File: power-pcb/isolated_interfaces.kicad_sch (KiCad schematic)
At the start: 24 parts, among them J10 USB_A, U16 RFM-0505S, U17 RFM-0505S, U18 RFM-0505S, U19 ECMF02-2AMX6, U20 ADUM3160

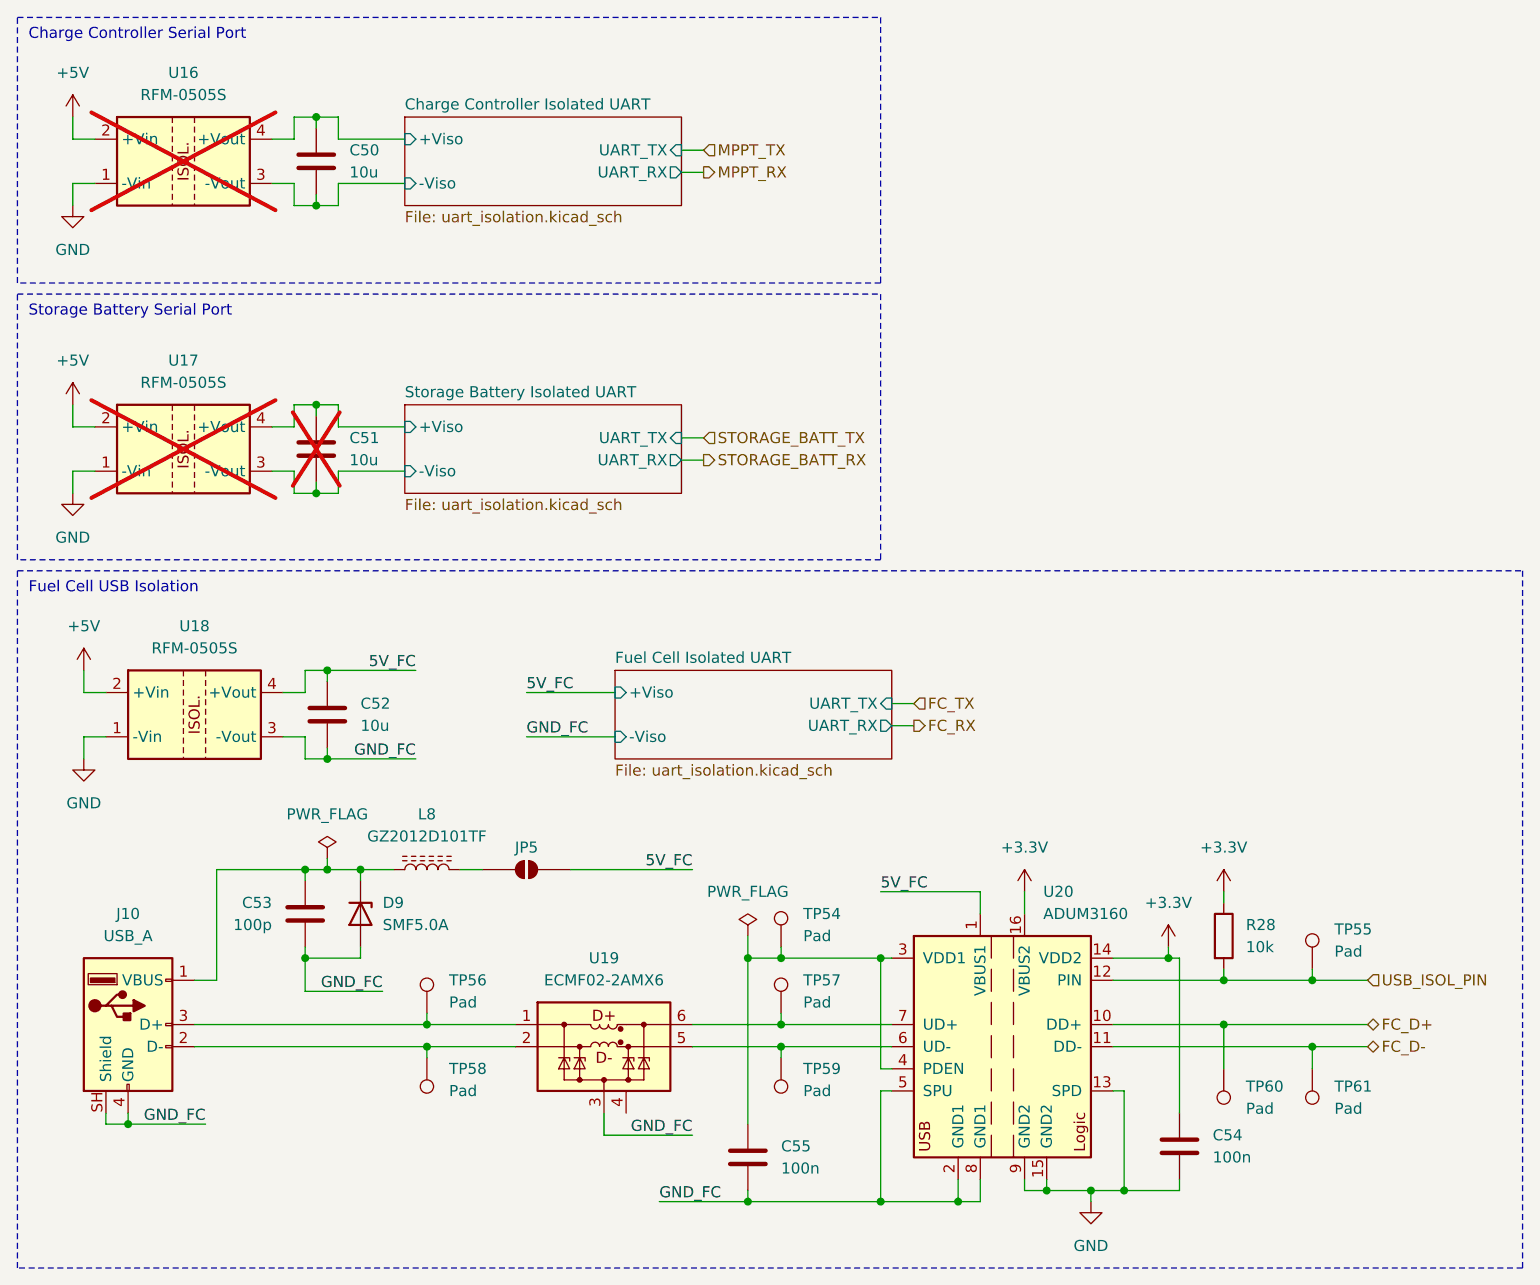
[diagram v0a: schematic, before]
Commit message: power-pcb: re-annotate schematic and start board
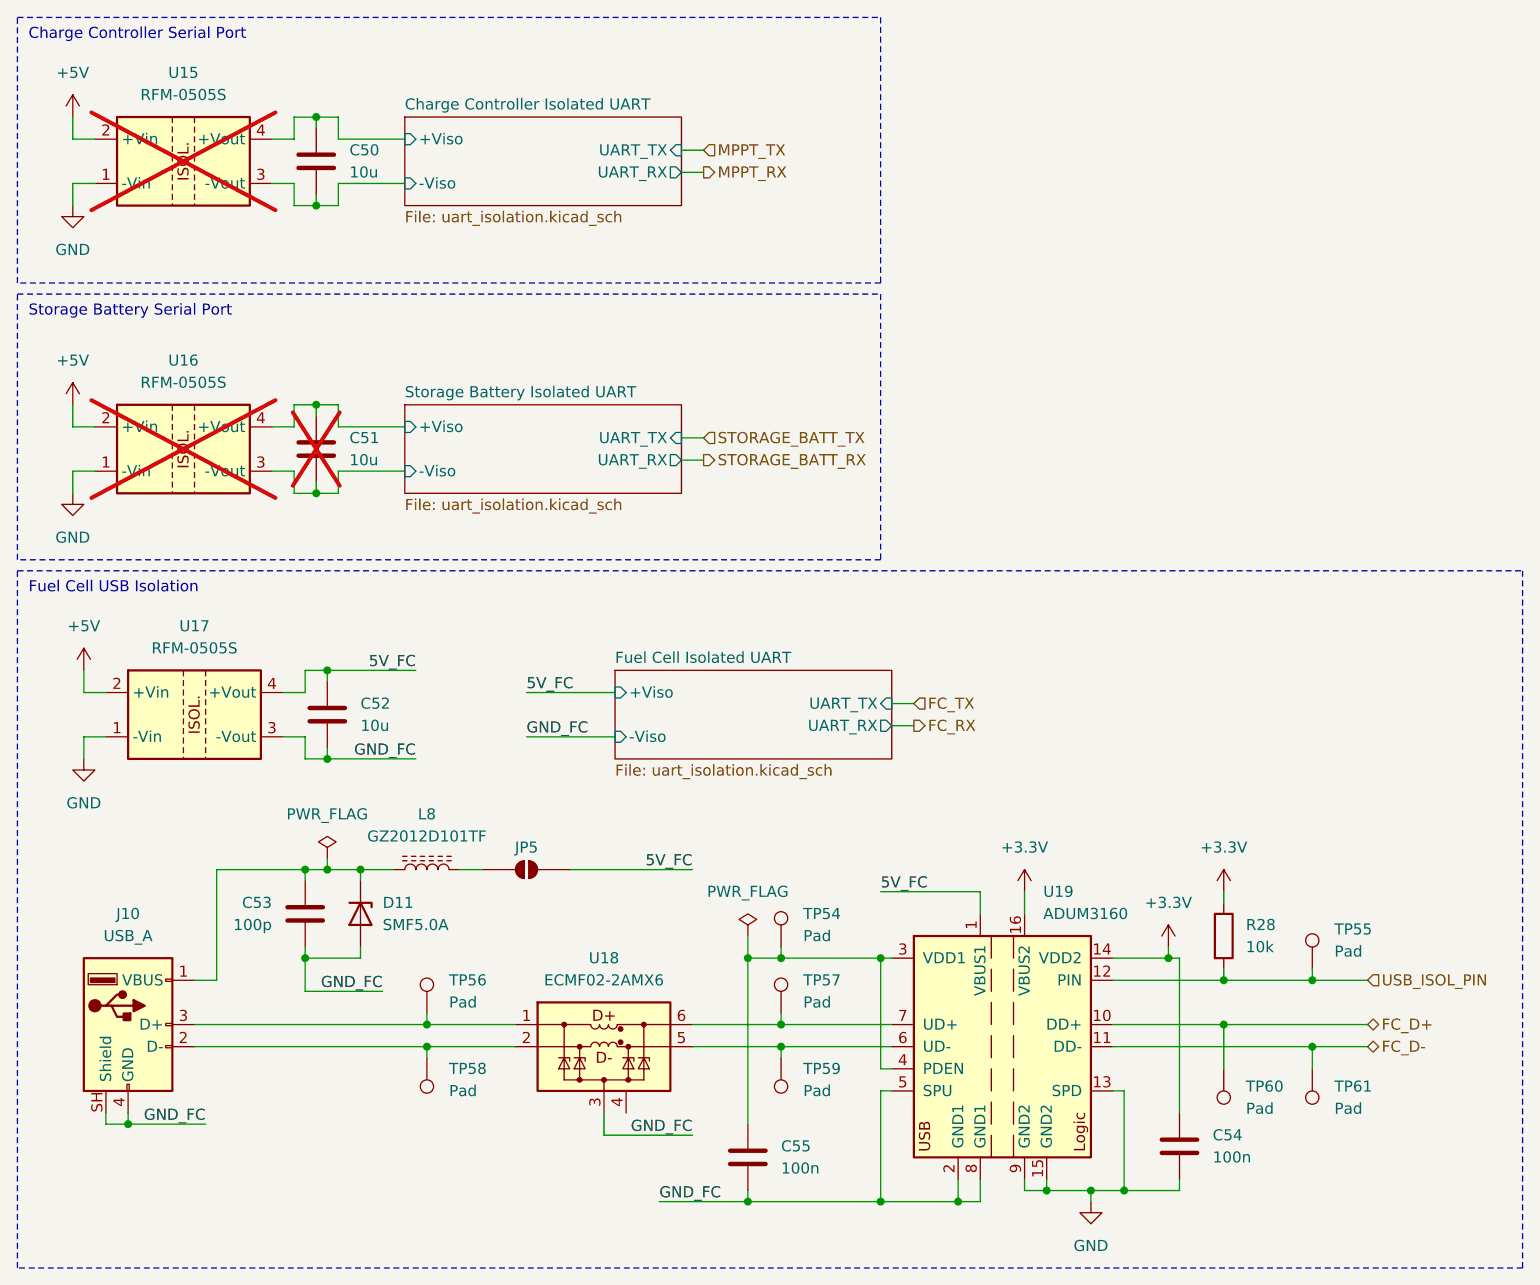
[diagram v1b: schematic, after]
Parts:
- renumbered D9 to D11, U16 to U15, U17 to U16, U18 to U17, U19 to U18, U20 to U19
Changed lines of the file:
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@@
 		(dnp no)
 		(fields_autoplaced yes)
-		(property "Reference" "D9"
+		(property "Reference" "D11"
 			(at 54.61 114.2999 90)
 			(show_name no)
@@
 			(project "power-pcb"
 				(path "/4b4cf3aa-c94c-4150-b9c5-35049cd71136/98c47c69-e753-45d5-a949-1f6e782e8c07"
-					(reference "D9")
+					(reference "D11")
 					(unit 1)
 					(variant
@@
 		(dnp no)
 		(fields_autoplaced yes)
-		(property "Reference" "U19"
+		(property "Reference" "U18"
 			(at 80.01 120.65 0)
 			(show_name no)
@@
 			(project "power-pcb"
 				(path "/4b4cf3aa-c94c-4150-b9c5-35049cd71136/98c47c69-e753-45d5-a949-1f6e782e8c07"
-					(reference "U19")
+					(reference "U18")
 					(unit 1)
 					(variant
@@
 		(dnp no)
 		(fields_autoplaced yes)
-		(property "Reference" "U18"
+		(property "Reference" "U17"
 			(at 33.02 82.55 0)
 			(show_name no)
@@
 			(project "power-pcb"
 				(path "/4b4cf3aa-c94c-4150-b9c5-35049cd71136/98c47c69-e753-45d5-a949-1f6e782e8c07"
-					(reference "U18")
+					(reference "U17")
 					(unit 1)
 					(variant
@@
 		(dnp yes)
 		(fields_autoplaced yes)
-		(property "Reference" "U17"
+		(property "Reference" "U16"
 			(at 31.75 52.07 0)
 			(show_name no)
@@
 			(project "power-pcb"
 				(path "/4b4cf3aa-c94c-4150-b9c5-35049cd71136/98c47c69-e753-45d5-a949-1f6e782e8c07"
-					(reference "U17")
+					(reference "U16")
 					(unit 1)
 					(variant
@@
 		(dnp no)
 		(fields_autoplaced yes)
-		(property "Reference" "U20"
+		(property "Reference" "U19"
 			(at 130.4133 113.03 0)
 			(show_name no)
@@
 			(project "power-pcb"
 				(path "/4b4cf3aa-c94c-4150-b9c5-35049cd71136/98c47c69-e753-45d5-a949-1f6e782e8c07"
-					(reference "U20")
+					(reference "U19")
 					(unit 1)
 					(variant
@@
 		(dnp yes)
 		(fields_autoplaced yes)
-		(property "Reference" "U16"
+		(property "Reference" "U15"
 			(at 31.75 19.05 0)
 			(show_name no)
@@
 			(project "power-pcb"
 				(path "/4b4cf3aa-c94c-4150-b9c5-35049cd71136/98c47c69-e753-45d5-a949-1f6e782e8c07"
-					(reference "U16")
+					(reference "U15")
 					(unit 1)
 					(variant

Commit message: power-pcb: fix schematic after review
- Add footprint for resitive load for the RECOM
- Add Opamps when useful
- Add capacitor and change some footprint sizes
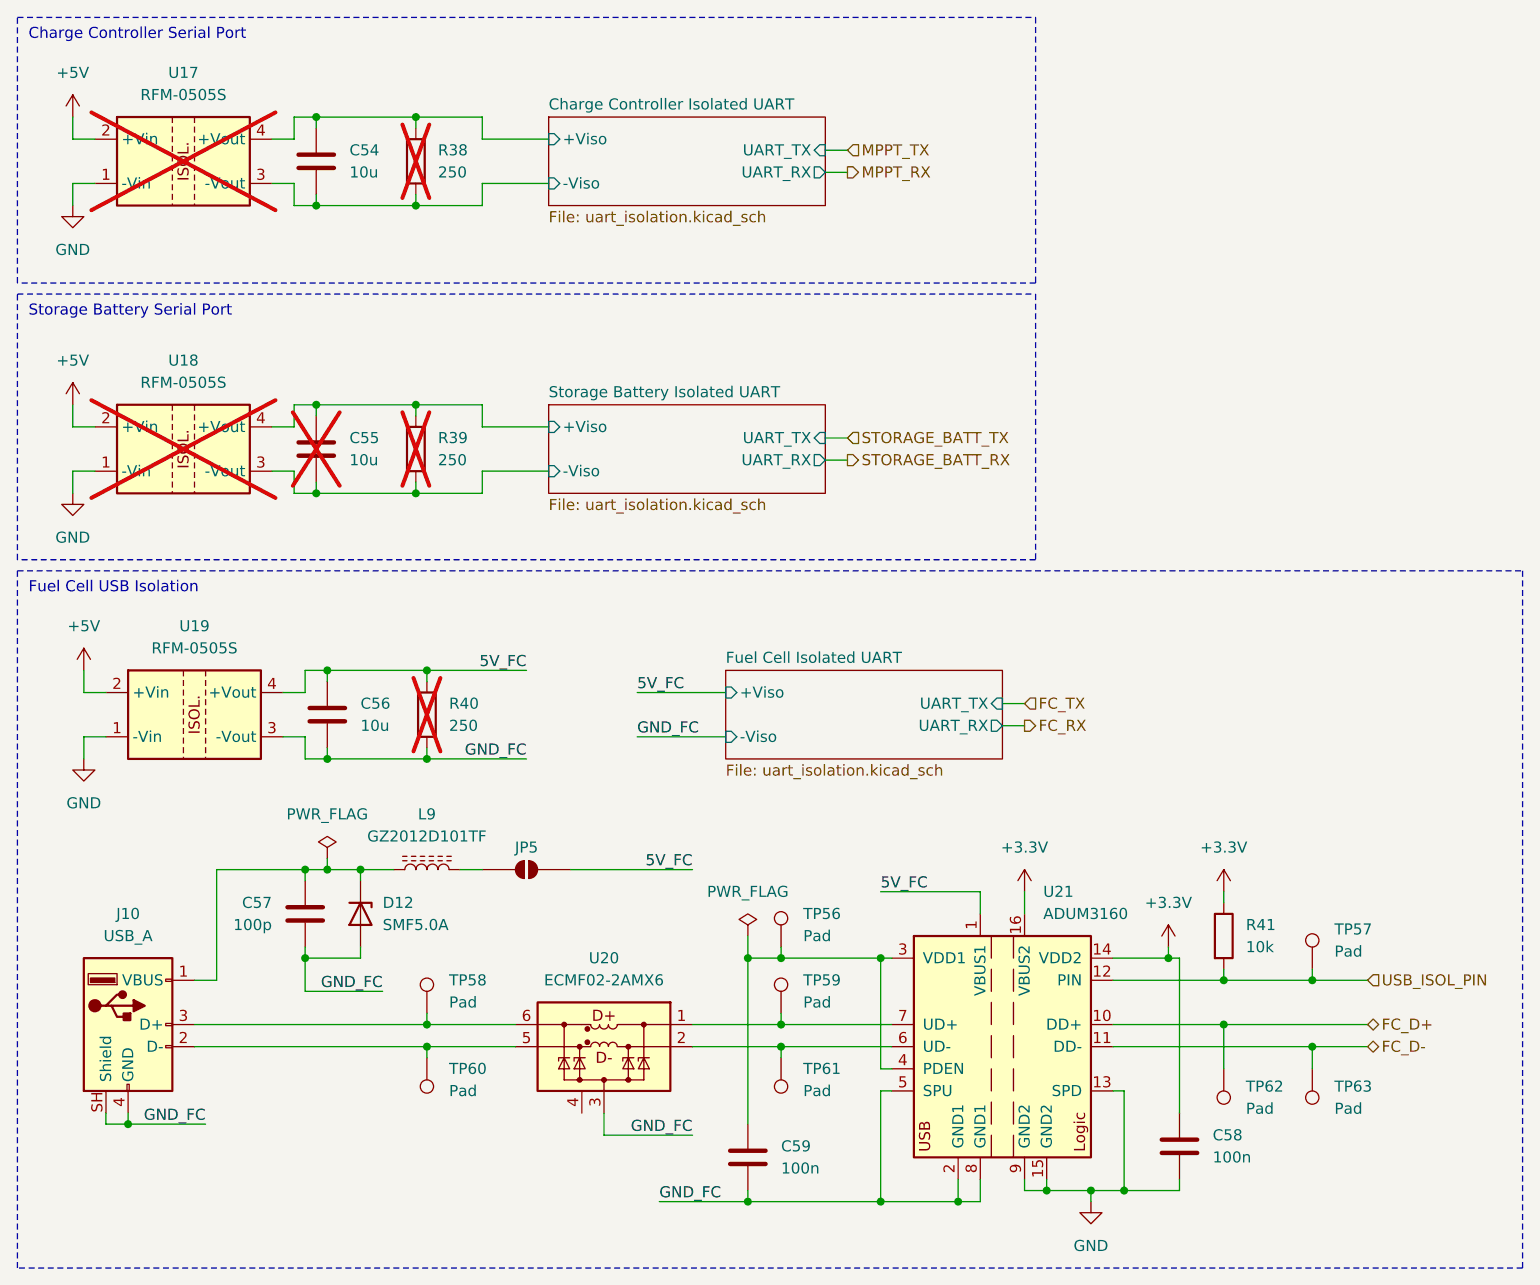
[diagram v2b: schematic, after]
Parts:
- added R38, R39, R40: 250, Resistor_THT:R_Axial_DIN0309_L9.0mm_D3.2mm_P12.70mm_Horizontal, symbol Device:R
- C58: renamed from C54; footprint Capacitor_SMD:C_0603_1608Metric_Pad1.08x0.95mm_HandSolder -> Capacitor_SMD:C_0402_1005Metric_Pad0.74x0.62mm_HandSolder; JLCPCB C14663 -> C307331
- C59: renamed from C55; footprint Capacitor_SMD:C_0603_1608Metric_Pad1.08x0.95mm_HandSolder -> Capacitor_SMD:C_0402_1005Metric_Pad0.74x0.62mm_HandSolder; JLCPCB C14663 -> C307331
- renumbered C50 to C54, C51 to C55, C52 to C56, C53 to C57, D11 to D12, L8 to L9, R28 to R41, TP54 to TP56, TP55 to TP57, TP56 to TP58, TP57 to TP59, TP58 to TP60, TP59 to TP61, TP60 to TP62, TP61 to TP63, U15 to U17, U16 to U18, U17 to U19, U18 to U20, U19 to U21
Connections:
- net 5V_FC: now also R40.1
- net Charge Controller Isolated UART/+Viso: now also R38.1
- net Charge Controller Isolated UART/-Viso: now also R38.2
- net GND_FC: now also R40.2
- net Storage Battery Isolated UART/+Viso: now also R39.1
- net Storage Battery Isolated UART/-Viso: now also R39.2
- net at J10.3 (D+), TP58.1: now also U20.6 (D+_out); no longer U20.1 (D+_in)
- net at J10.2 (D-), TP60.1: now also U20.5 (D-_out); no longer U20.2 (D-_in)
- net at TP61.1, U21.6 (UD-): now also U20.2 (D-_in); no longer U20.5 (D-_out)
- net at TP59.1, U21.7 (UD+): now also U20.1 (D+_in); no longer U20.6 (D+_out)

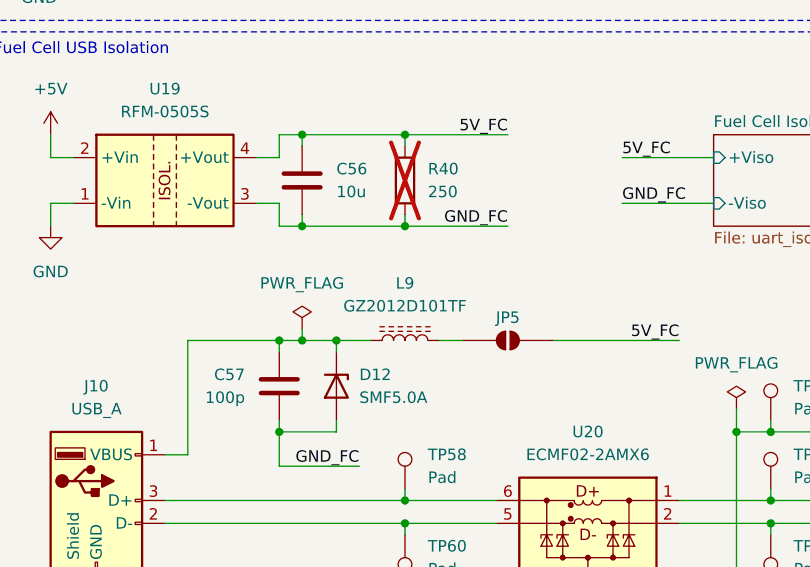
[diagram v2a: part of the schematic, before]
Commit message: power-pcb: work on part placement and JLCPCB DNP
Some of the components that were recentlt added had not been marked as
DNP for JLCPCB yet, this is now done.
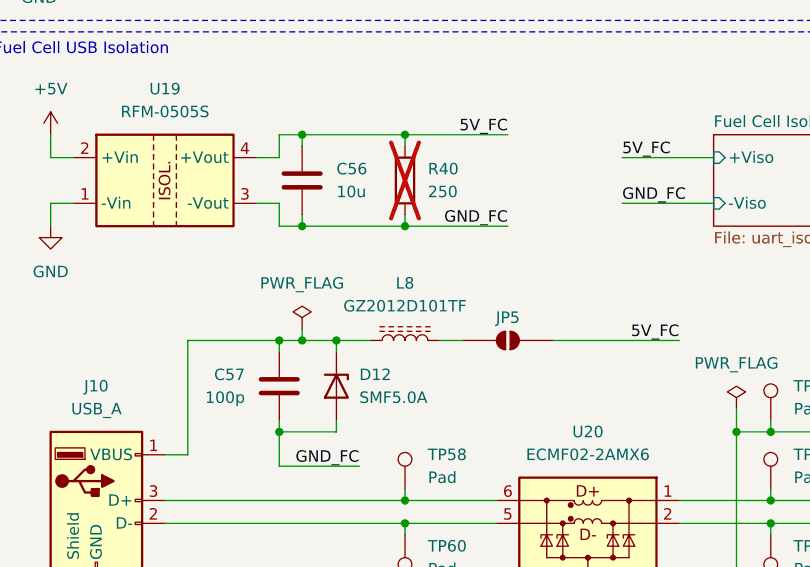
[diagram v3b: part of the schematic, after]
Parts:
- renumbered L9 to L8
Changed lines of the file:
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@@
 		(dnp no)
 		(fields_autoplaced yes)
-		(property "Reference" "L9"
+		(property "Reference" "L8"
 			(at 59.69 104.14 90)
 			(show_name no)
@@
 			(project "power-pcb"
 				(path "/4b4cf3aa-c94c-4150-b9c5-35049cd71136/98c47c69-e753-45d5-a949-1f6e782e8c07"
-					(reference "L9")
+					(reference "L8")
 					(unit 1)
 					(variant

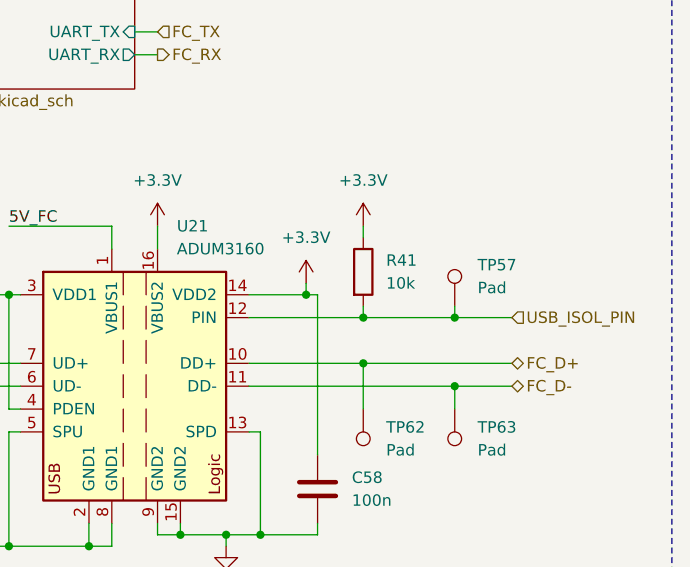
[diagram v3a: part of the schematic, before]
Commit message: power-pcb: change some 10k to 12k
JLCPCB doesn't offer a small package for the 10k resistors so some had
to be changed.
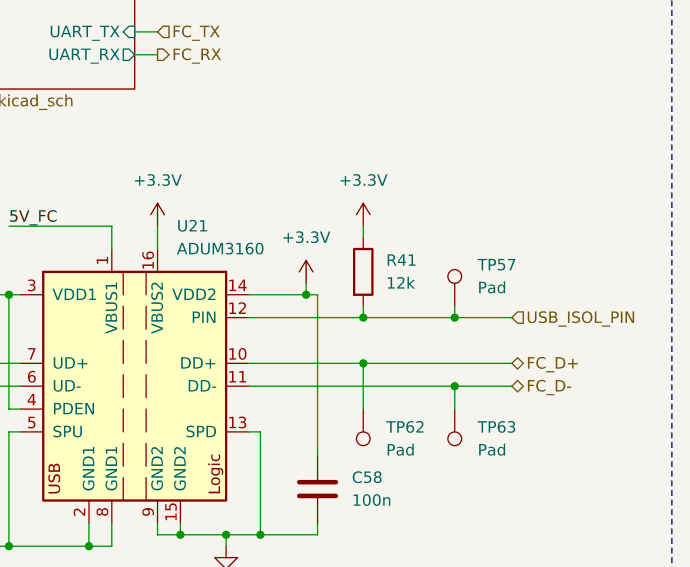
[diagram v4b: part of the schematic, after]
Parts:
- R41: value 10k -> 12k; footprint Resistor_SMD:R_0603_1608Metric_Pad0.98x0.95mm_HandSolder -> Resistor_SMD:R_0402_1005Metric_Pad0.72x0.64mm_HandSolder; JLCPCB C25804 -> C25752
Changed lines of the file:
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@@
 	(title_block
 		(title "Isolated Interfaces")
-		(date "2026-06-13")
+		(date "2026-06-17")
 		(rev "v1.1.0")
 	)
@@
 			)
 		)
-		(property "Value" "10k"
+		(property "Value" "12k"
 			(at 153.67 119.3799 0)
 			(show_name no)
@@
 			)
 		)
-		(property "Footprint" "Resistor_SMD:R_0603_1608Metric_Pad0.98x0.95mm_HandSolder"
+		(property "Footprint" "Resistor_SMD:R_0402_1005Metric_Pad0.72x0.64mm_HandSolder"
 			(at 149.352 118.11 90)
 			(hide yes)
@@
 			)
 		)
-		(property "JLCPCB" "C25804"
+		(property "JLCPCB" "C25752"
 			(at 151.13 118.11 0)
 			(hide yes)
